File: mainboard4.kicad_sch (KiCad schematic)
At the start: 12 parts, among them J13 USB_C_Receptacle_USB2.0_16P, J8 Barrel_Jack

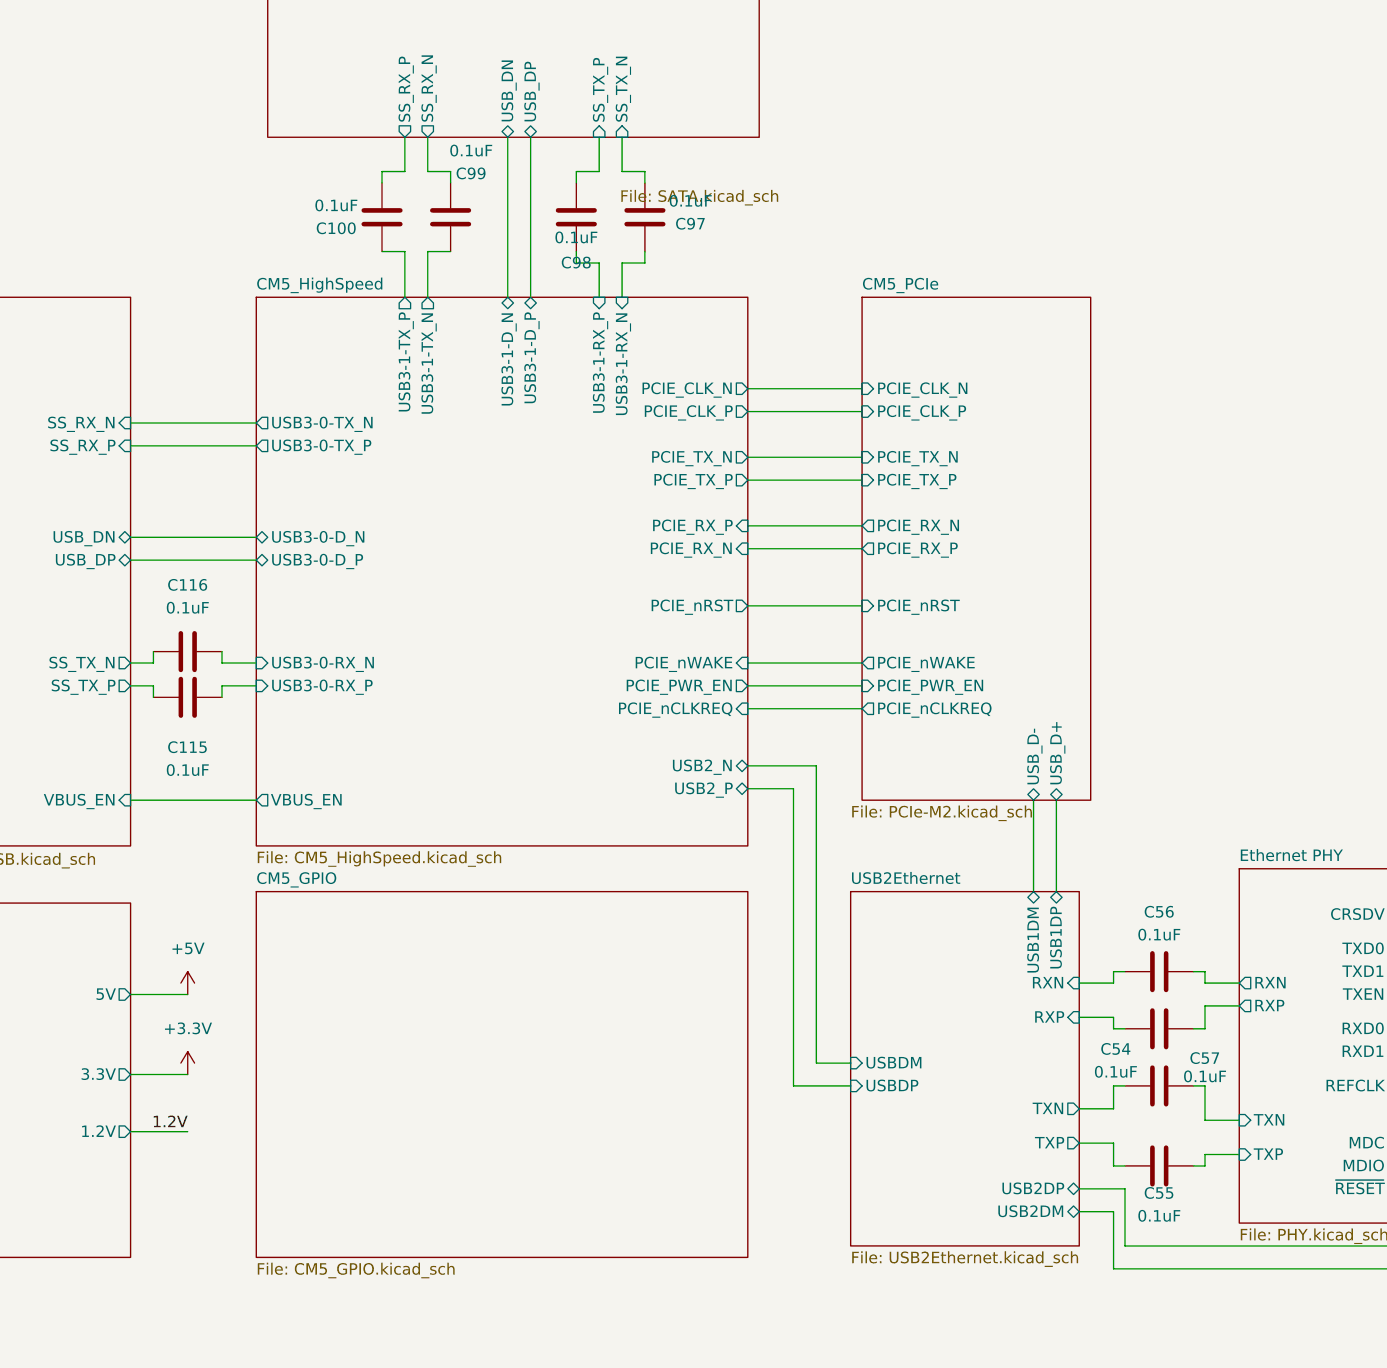
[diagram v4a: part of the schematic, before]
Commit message: add sata capacitor
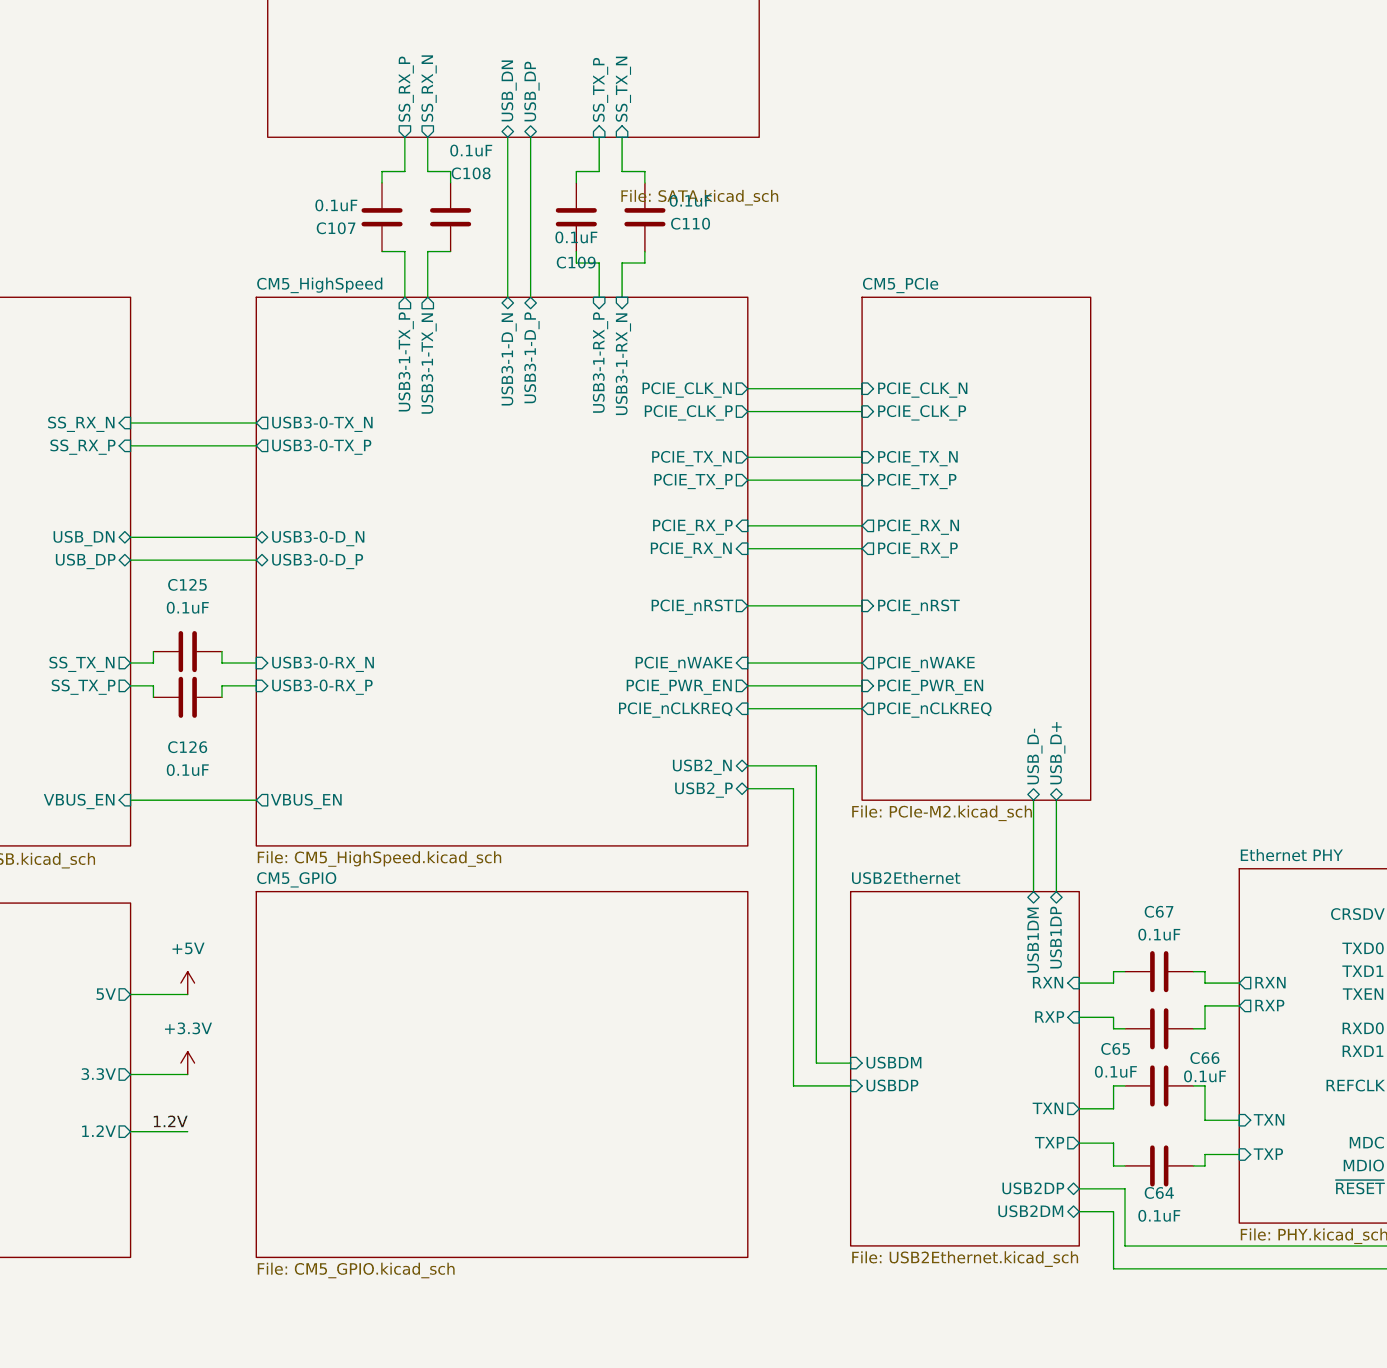
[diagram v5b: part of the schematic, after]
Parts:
- renumbered C100 to C107, C99 to C108, C98 to C109, C97 to C110, C116 to C125, C115 to C126, C55 to C64, C54 to C65, C57 to C66, C56 to C67
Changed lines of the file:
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@@
 	(label "1.2V"
 		(at 41.91 104.14 0)
+		(fields_autoplaced yes)
 		(effects
 			(font
@@
 	(label "1.2V"
 		(at 87.63 148.59 180)
+		(fields_autoplaced yes)
 		(effects
 			(font
@@
 		(on_board yes)
 		(dnp no)
-		(property "Reference" "C115"
+		(property "Reference" "C126"
 			(at 87.63 105.918 90)
 			(effects
@@
 			(project "mainboard4"
 				(path "/dd07ab80-a59c-44f4-ac7d-849e21e1384e"
-					(reference "C115")
+					(reference "C126")
 					(unit 1)
 				)
@@
 		(on_board yes)
 		(dnp no)
-		(property "Reference" "C99"
+		(property "Reference" "C108"
 			(at 119.126 42.164 0)
 			(effects
@@
 			(project "mainboard4"
 				(path "/dd07ab80-a59c-44f4-ac7d-849e21e1384e"
-					(reference "C99")
+					(reference "C108")
 					(unit 1)
 				)
@@
 		(on_board yes)
 		(dnp no)
-		(property "Reference" "C116"
+		(property "Reference" "C125"
 			(at 87.63 87.884 90)
 			(effects
@@
 			(project "mainboard4"
 				(path "/dd07ab80-a59c-44f4-ac7d-849e21e1384e"
-					(reference "C116")
+					(reference "C125")
 					(unit 1)
 				)
@@
 		(on_board yes)
 		(dnp no)
-		(property "Reference" "C55"
+		(property "Reference" "C64"
 			(at 195.58 155.448 90)
 			(effects
@@
 			(project "mainboard4"
 				(path "/dd07ab80-a59c-44f4-ac7d-849e21e1384e"
-					(reference "C55")
+					(reference "C64")
 					(unit 1)
 				)
@@
 		(on_board yes)
 		(dnp no)
-		(property "Reference" "C56"
+		(property "Reference" "C67"
 			(at 195.58 124.206 90)
 			(effects
@@
 			(project "mainboard4"
 				(path "/dd07ab80-a59c-44f4-ac7d-849e21e1384e"
-					(reference "C56")
+					(reference "C67")
 					(unit 1)
 				)
@@
 		(on_board yes)
 		(dnp no)
-		(property "Reference" "C97"
+		(property "Reference" "C110"
 			(at 143.51 47.752 0)
 			(effects
@@
 			(project "mainboard4"
 				(path "/dd07ab80-a59c-44f4-ac7d-849e21e1384e"
-					(reference "C97")
+					(reference "C110")
 					(unit 1)
 				)
@@
 		(on_board yes)
 		(dnp no)
-		(property "Reference" "C100"
+		(property "Reference" "C107"
 			(at 104.14 48.26 0)
 			(effects
@@
 			(project "mainboard4"
 				(path "/dd07ab80-a59c-44f4-ac7d-849e21e1384e"
-					(reference "C100")
+					(reference "C107")
 					(unit 1)
 				)
@@
 		(on_board yes)
 		(dnp no)
-		(property "Reference" "C54"
+		(property "Reference" "C65"
 			(at 190.754 139.446 90)
 			(effects
@@
 			(project "mainboard4"
 				(path "/dd07ab80-a59c-44f4-ac7d-849e21e1384e"
-					(reference "C54")
+					(reference "C65")
 					(unit 1)
 				)
@@
 		(on_board yes)
 		(dnp no)
-		(property "Reference" "C98"
+		(property "Reference" "C109"
 			(at 130.81 52.07 0)
 			(effects
@@
 			(project "mainboard4"
 				(path "/dd07ab80-a59c-44f4-ac7d-849e21e1384e"
-					(reference "C98")
+					(reference "C109")
 					(unit 1)
 				)
@@
 		(on_board yes)
 		(dnp no)
-		(property "Reference" "C57"
+		(property "Reference" "C66"
 			(at 200.66 140.462 90)
 			(effects
@@
 			(project "mainboard4"
 				(path "/dd07ab80-a59c-44f4-ac7d-849e21e1384e"
-					(reference "C57")
-					(unit 1)
-				)
+					(reference "C66")
+					(unit 1)
+				)

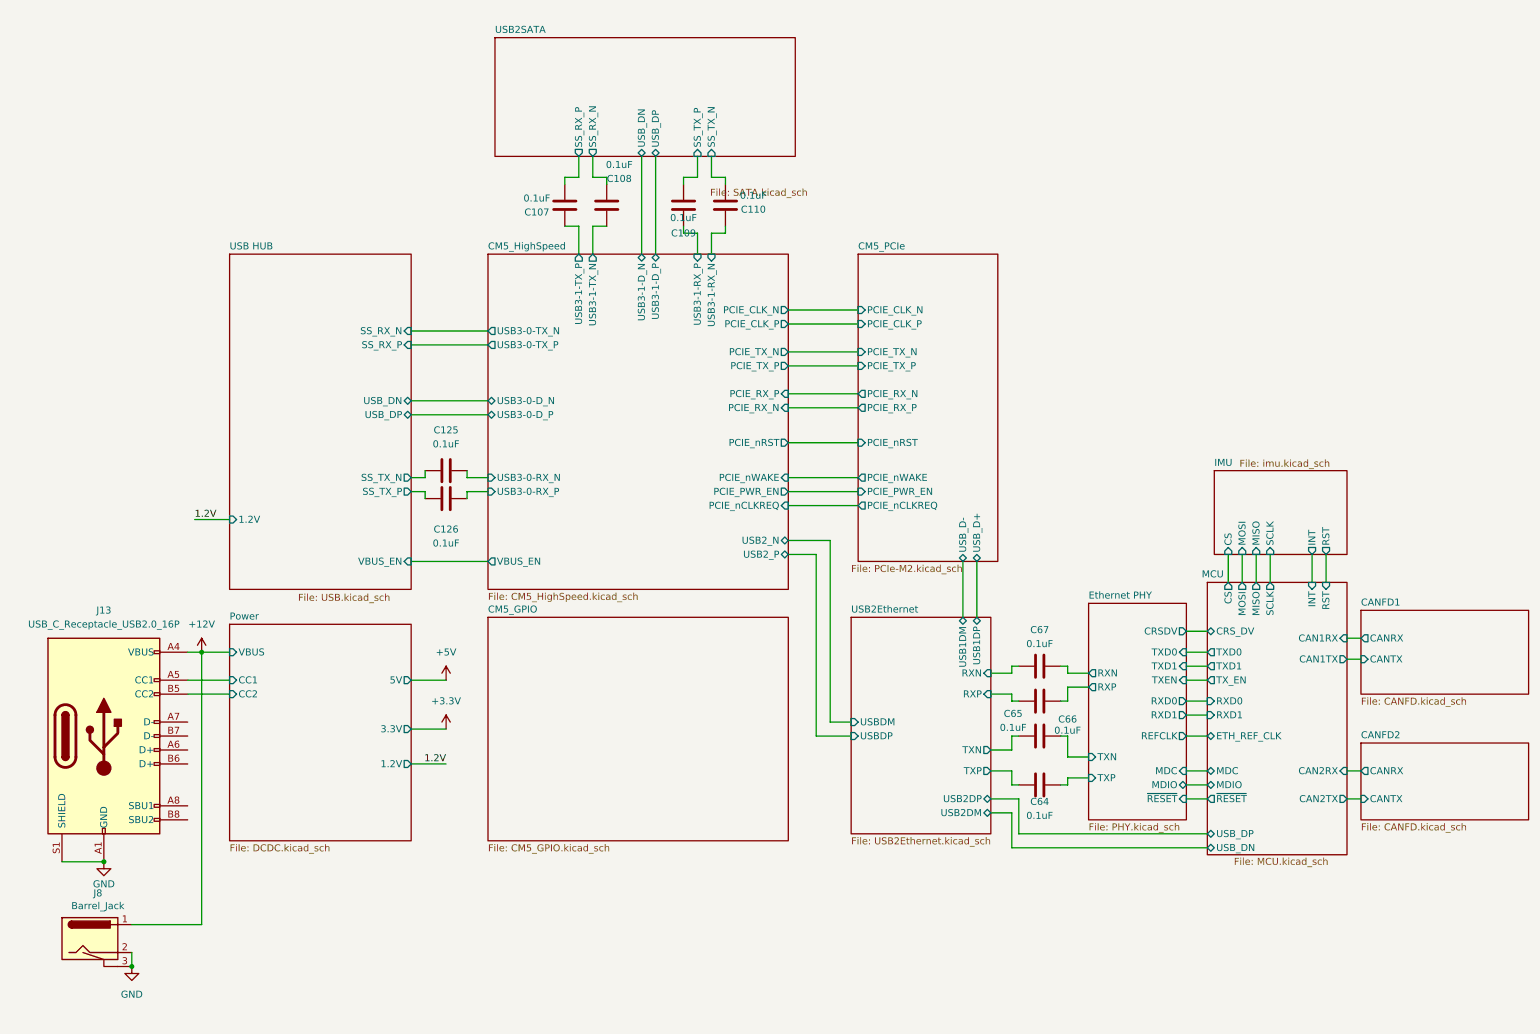
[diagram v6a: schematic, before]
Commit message: delete usb hub
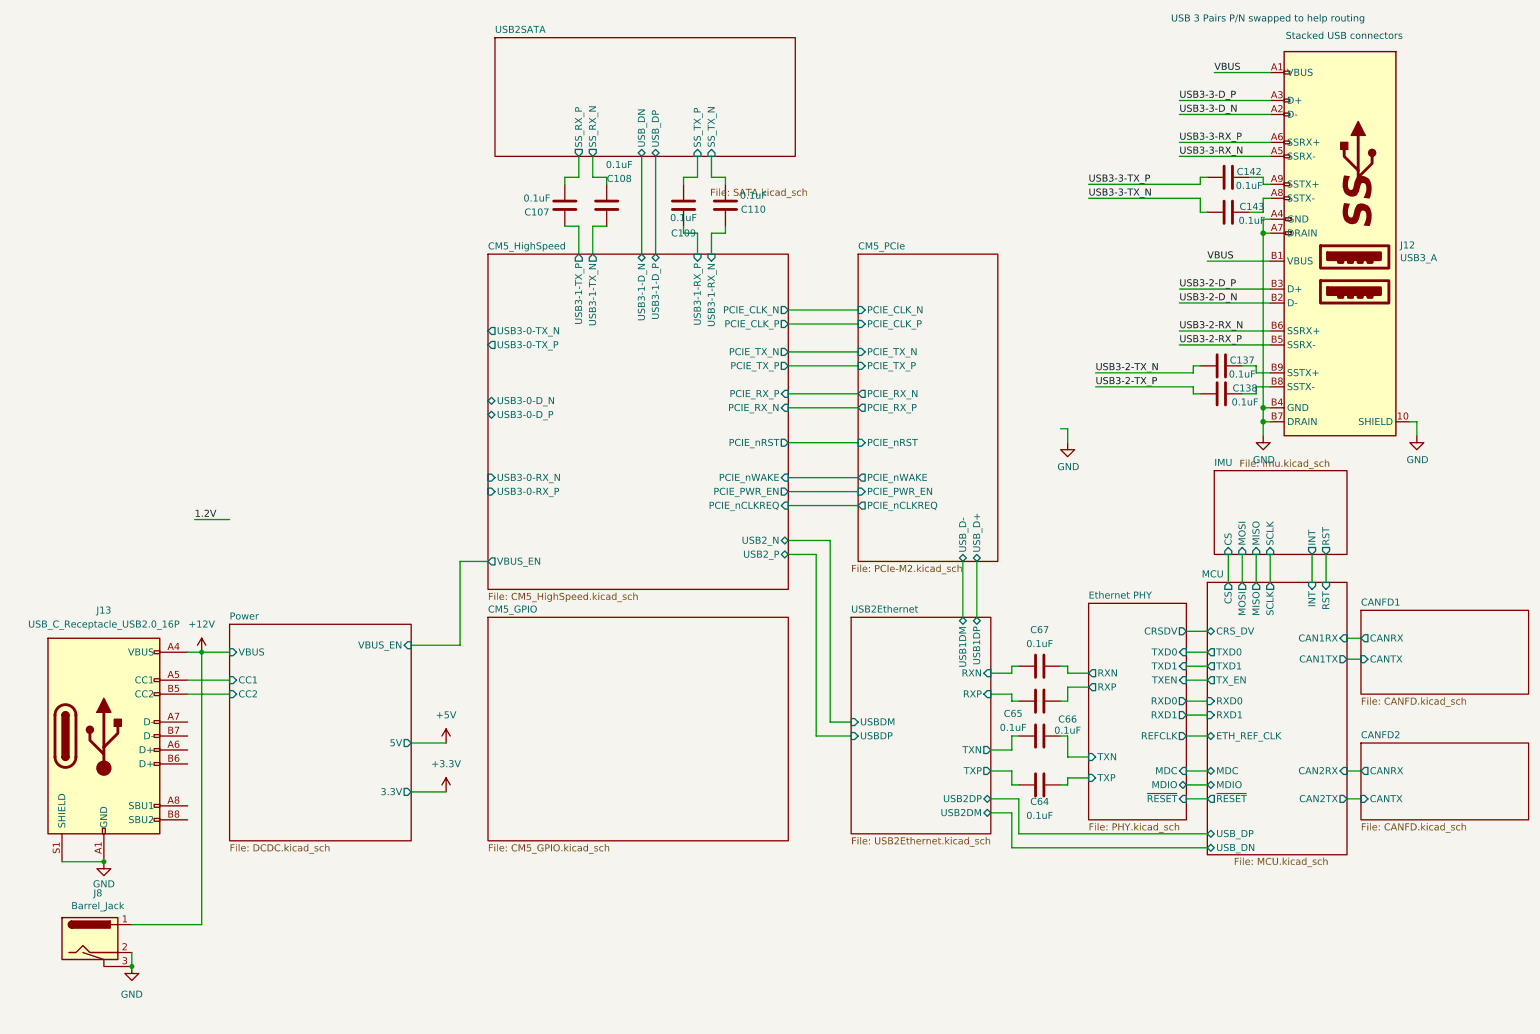
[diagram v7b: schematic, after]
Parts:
- removed C125, C126: 0.1uF, Capacitor_SMD:C_0402_1005Metric_Pad0.74x0.62mm_HandSolder, symbol Device:C
- added C137, C138, C142, C143: 0.1uF, Capacitor_SMD:C_0402_1005Metric_Pad0.74x0.62mm_HandSolder, symbol Device:C
- added J12: USB3_A, CM5IO:MTCONN_UBAF30-D2011, symbol CM5IO:USB3_A
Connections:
- net GND: now also J12.10 (SHIELD), J12.A4 (GND), J12.A7 (DRAIN), J12.B4 (GND), J12.B7 (DRAIN)
- new net: C138.2, J12.B8 (SSTX-)
- new net: C137.2, J12.B9 (SSTX+)
- new net: C143.2, J12.A8 (SSTX-)
- new net: C142.2, J12.A9 (SSTX+)
- new net USB3-2-D_N: J12.B2 (D-)
- new net USB3-2-D_P: J12.B3 (D+)
- new net USB3-2-RX_N: J12.B6 (SSRX+)
- new net USB3-2-RX_P: J12.B5 (SSRX-)
- new net USB3-2-TX_N: C137.1
- new net USB3-2-TX_P: C138.1
- new net USB3-3-D_N: J12.A2 (D-)
- new net USB3-3-D_P: J12.A3 (D+)
- new net USB3-3-RX_N: J12.A5 (SSRX-)
- new net USB3-3-RX_P: J12.A6 (SSRX+)
- new net USB3-3-TX_N: C143.1
- new net USB3-3-TX_P: C142.1
- new net VBUS: J12.A1 (VBUS), J12.B1 (VBUS)
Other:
- removed sheet USB HUB
- sheet Power ports: added VBUS_EN; removed 1.2V
- note added: "Stacked USB connectors"
- note added: "USB 3 Pairs P/N swapped to help routing"

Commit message: delete USB connector
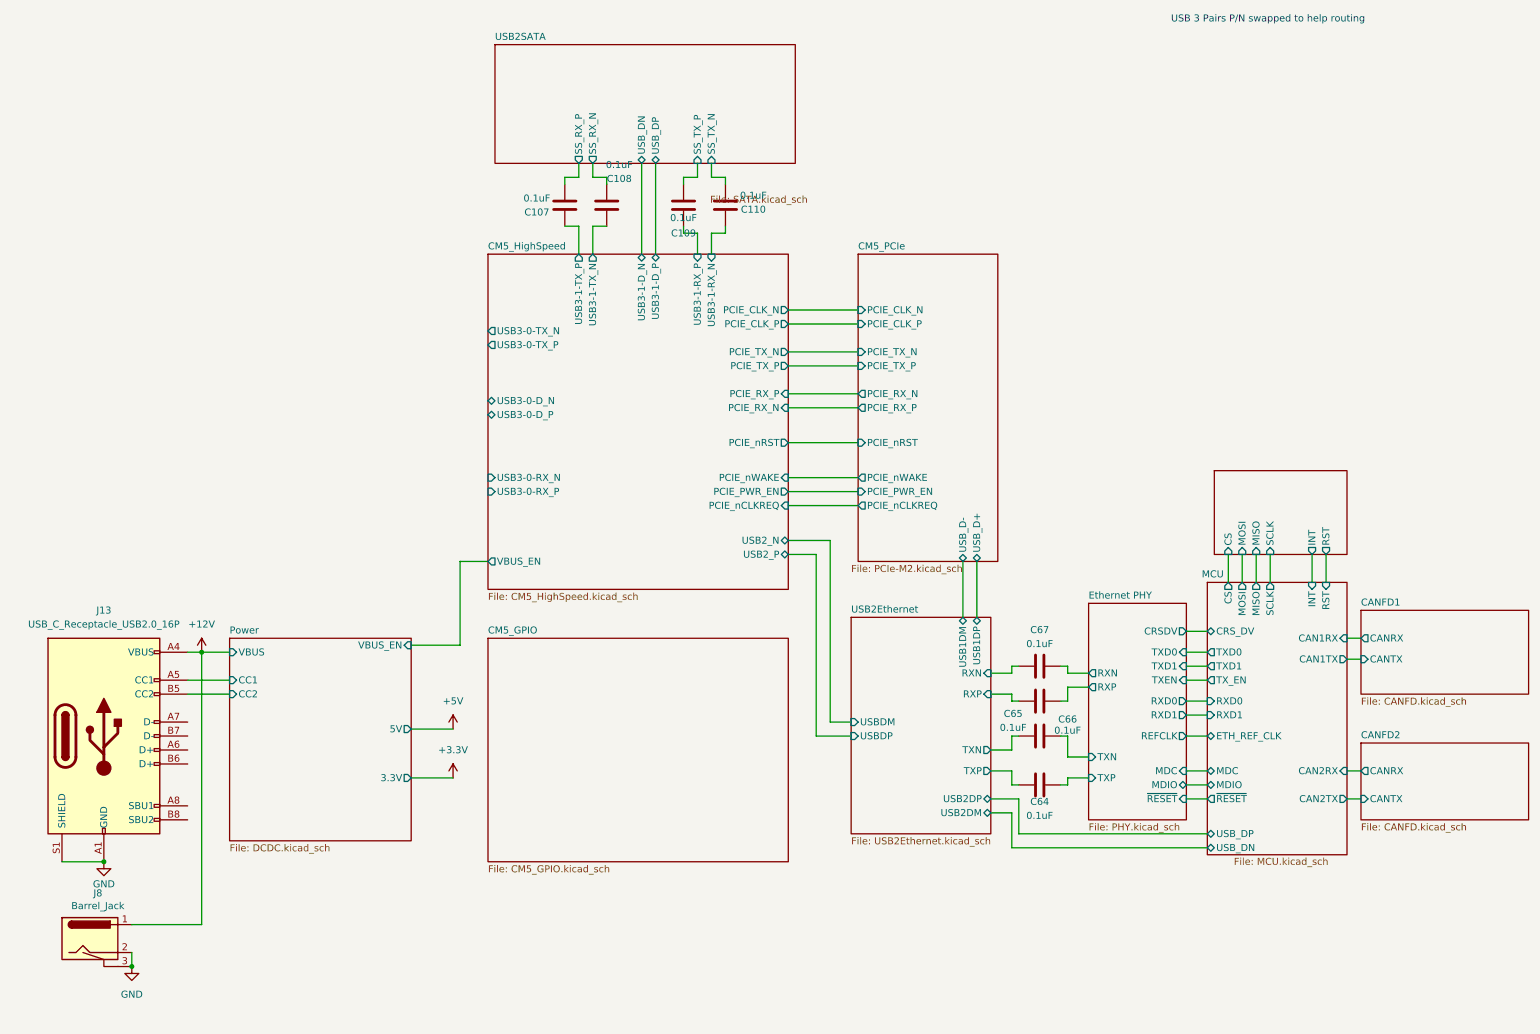
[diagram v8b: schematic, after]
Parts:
- removed C137, C138, C142, C143: 0.1uF, Capacitor_SMD:C_0402_1005Metric_Pad0.74x0.62mm_HandSolder, symbol Device:C
- removed J12: USB3_A, CM5IO:MTCONN_UBAF30-D2011, symbol CM5IO:USB3_A
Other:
- note removed: "Stacked USB connectors"
